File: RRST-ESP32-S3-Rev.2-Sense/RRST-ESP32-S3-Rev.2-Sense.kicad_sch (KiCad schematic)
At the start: 41 parts, among them J1 Conn_01x22_Pin, J10 Conn_01x02_Socket, J11 Conn_01x02_Socket, J12 Conn_01x02_Socket, J2 USB_C_Receptacle_USB2.0_16P, J3 Conn_01x22_Pin, J4 Conn_01x04_Socket, J5 Conn_01x04_Socket, J6 Conn_01x04_Socket, J7 Conn_01x04_Socket, J8 Conn_01x04_Socket, J9 Conn_01x02_Socket, SW1 SW_Push, SW2 SW_Push, U1 ESP32-S3-WROOM-1, U2 LD1117S33TR_SOT223, U4 MCP2561-E-SN

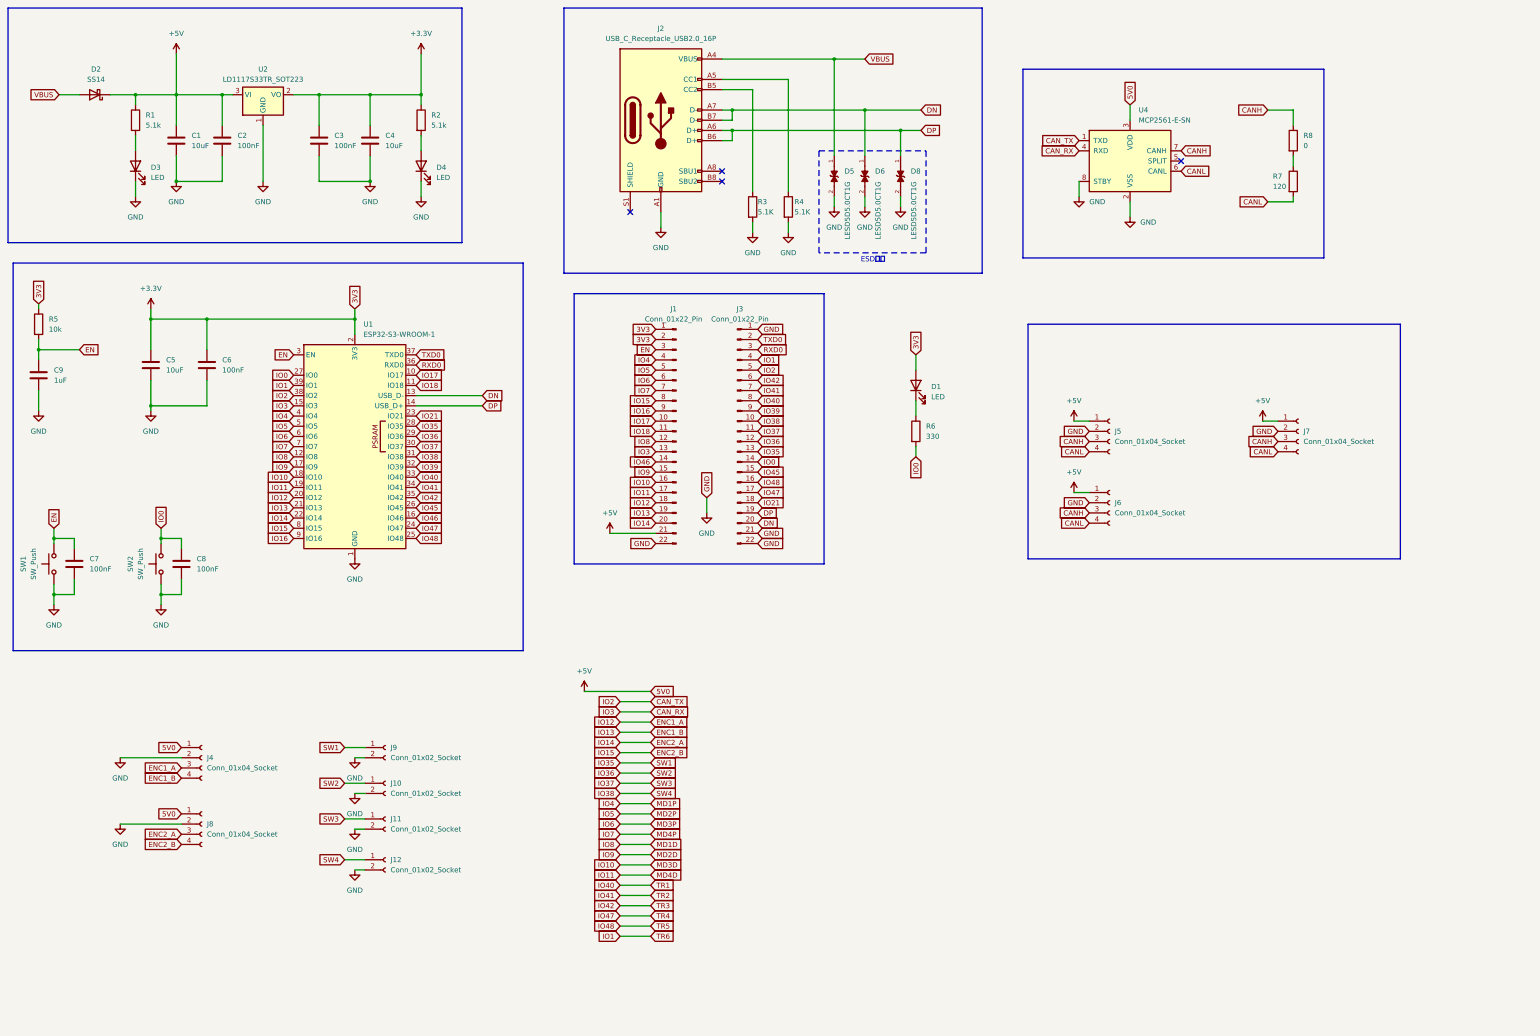
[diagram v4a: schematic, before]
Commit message: 仮配置完了、拡張基板設計開始
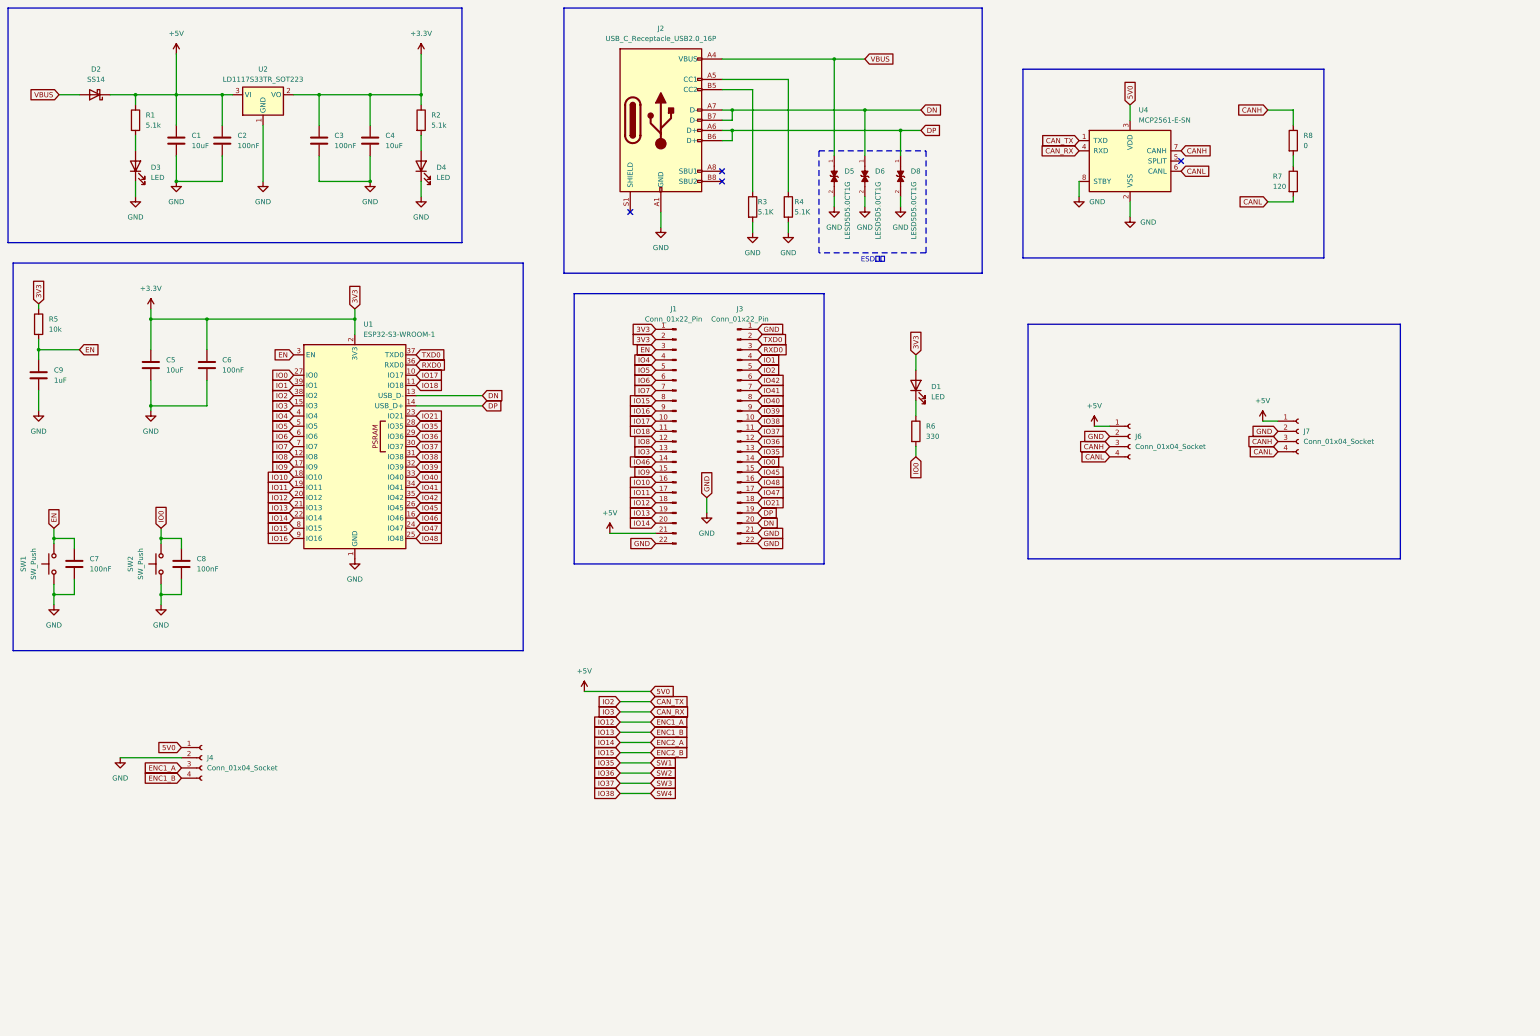
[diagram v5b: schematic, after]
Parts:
- removed J10, J11, J12, J9: Conn_01x02_Socket, Connector_JST:JST_XH_B2B-XH-A_1x02_P2.50mm_Vertical, symbol Connector:Conn_01x02_Socket
- removed J5, J8: Conn_01x04_Socket, Connector_JST:JST_XH_B4B-XH-A_1x04_P2.50mm_Vertical, symbol Connector:Conn_01x04_Socket
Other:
- moved on the sheet: J6
